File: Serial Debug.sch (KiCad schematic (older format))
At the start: 19 parts

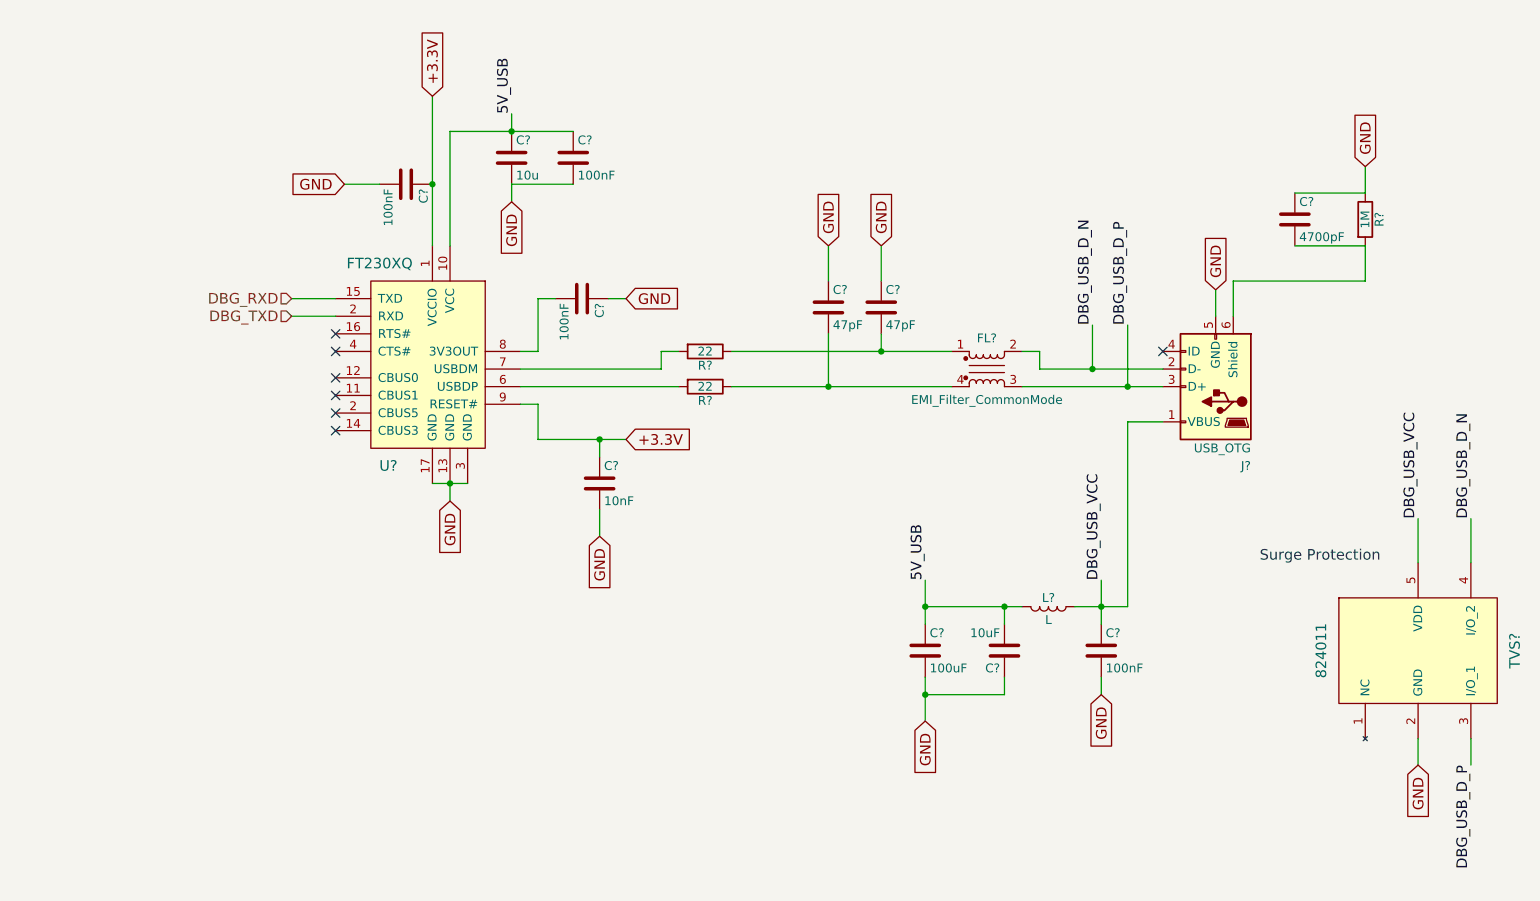
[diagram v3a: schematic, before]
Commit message: some issues fixed by the bugfixer; formal verification needed
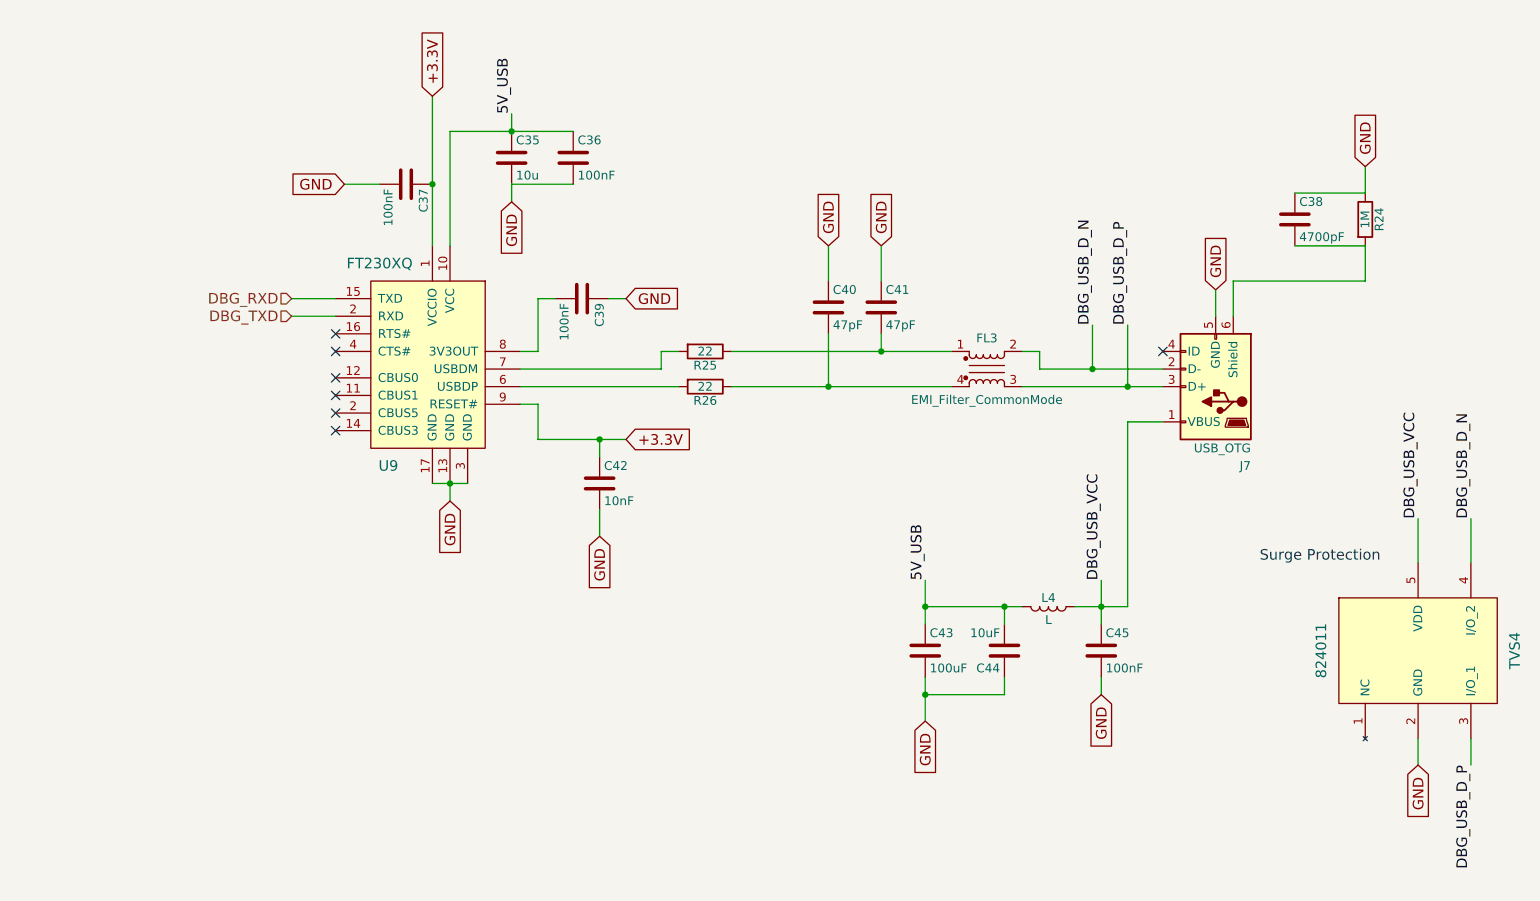
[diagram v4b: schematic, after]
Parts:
- gave numbers to parts that had none: 19
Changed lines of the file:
@@
 $EndDescr
 $Comp
-L FT230XQ U?
+L FT230XQ U9
 U 1 1 59A28254
 P 2450 2100
-F 0 "U?" H 2550 400 60  0000 C CNN
+F 0 "U9" H 2550 400 60  0000 C CNN
 F 1 "FT230XQ" H 2600 1550 60  0000 C CNN
 F 2 "" H 2450 2100 60  0001 C CNN
@@
 	3200 3450 3200 3650
 $Comp
-L R R?
+L R R25
 U 1 1 59A2A431
 P 4150 3150
-F 0 "R?" V 4230 3150 50  0000 C CNN
+F 0 "R25" V 4230 3150 50  0000 C CNN
 F 1 "22" V 4150 3150 50  0000 C CNN
 F 2 "" V 4080 3150 50  0001 C CNN
@@
 $EndComp
 $Comp
-L R R?
+L R R26
 U 1 1 59A2A466
 P 4150 3350
-F 0 "R?" V 4230 3350 50  0000 C CNN
+F 0 "R26" V 4230 3350 50  0000 C CNN
 F 1 "22" V 4150 3350 50  0000 C CNN
 F 2 "" V 4080 3350 50  0001 C CNN
@@
 $EndComp
 $Comp
-L EMI_Filter_CommonMode FL?
+L EMI_Filter_CommonMode FL3
 U 1 1 59A2AADC
 P 5750 3250
-F 0 "FL?" H 5750 3425 50  0000 C CNN
+F 0 "FL3" H 5750 3425 50  0000 C CNN
 F 1 "EMI_Filter_CommonMode" H 5750 3075 50  0000 C CNN
 F 2 "" V 5750 3290 50  0000 C CNN
@@
 	3100 3250 3900 3250
 $Comp
-L USB_OTG J?
+L USB_OTG J7
 U 1 1 59A2B35A
 P 7050 3350
-F 0 "J?" H 6850 3800 50  0000 L CNN
+F 0 "J7" H 6850 3800 50  0000 L CNN
 F 1 "USB_OTG" H 6850 3700 50  0000 L CNN
 F 2 "" H 7200 3300 50  0001 C CNN
@@
 GND
 $Comp
-L C C?
+L C C38
 U 1 1 59A2C300
 P 7500 2400
-F 0 "C?" H 7525 2500 50  0000 L CNN
+F 0 "C38" H 7525 2500 50  0000 L CNN
 F 1 "4700pF" H 7525 2300 50  0000 L CNN
 F 2 "" H 7538 2250 50  0001 C CNN
@@
 $EndComp
 $Comp
-L R R?
+L R R24
 U 1 1 59A2C331
 P 7900 2400
-F 0 "R?" V 7980 2400 50  0000 C CNN
+F 0 "R24" V 7980 2400 50  0000 C CNN
 F 1 "1M" V 7900 2400 50  0000 C CNN
 F 2 "" V 7830 2400 50  0001 C CNN
@@
 NoConn ~ 6750 3150
 $Comp
-L C C?
+L C C43
 U 1 1 59A2D00A
 P 5400 4850
-F 0 "C?" H 5425 4950 50  0000 L CNN
+F 0 "C43" H 5425 4950 50  0000 L CNN
 F 1 "100uF" H 5425 4750 50  0000 L CNN
 F 2 "" H 5438 4700 50  0001 C CNN
@@
 $EndComp
 $Comp
-L L L?
+L L L4
 U 1 1 59A2D09D
 P 6100 4600
-F 0 "L?" V 6050 4600 50  0000 C CNN
+F 0 "L4" V 6050 4600 50  0000 C CNN
 F 1 "L" V 6175 4600 50  0000 C CNN
 F 2 "" H 6100 4600 50  0001 C CNN
@@
 GND
 $Comp
-L C C?
+L C C41
 U 1 1 59A2FBBD
 P 5150 2900
-F 0 "C?" H 5175 3000 50  0000 L CNN
+F 0 "C41" H 5175 3000 50  0000 L CNN
 F 1 "47pF" H 5175 2800 50  0000 L CNN
 F 2 "" H 5188 2750 50  0001 C CNN
@@
 $EndComp
 $Comp
-L C C?
+L C C40
 U 1 1 59A2FC88
 P 4850 2900
-F 0 "C?" H 4875 3000 50  0000 L CNN
+F 0 "C40" H 4875 3000 50  0000 L CNN
 F 1 "47pF" H 4875 2800 50  0000 L CNN
 F 2 "" H 4888 2750 50  0001 C CNN
@@
 Connection ~ 4850 3350
 $Comp
-L 824011 TVS?
+L 824011 TVS4
 U 1 1 59A30AB4
 P 9050 4800
-F 0 "TVS?" V 8750 4750 60  0000 C CNN
+F 0 "TVS4" V 8750 4750 60  0000 C CNN
 F 1 "824011" V 7650 4750 60  0000 C CNN
 F 2 "" H 9050 4800 60  0001 C CNN
@@
 5V_USB
 $Comp
-L C C?
+L C C35
 U 1 1 59A63DF8
 P 3050 2050
-F 0 "C?" H 3075 2150 50  0000 L CNN
+F 0 "C35" H 3075 2150 50  0000 L CNN
 F 1 "10u" H 3075 1950 50  0000 L CNN
 F 2 "" H 3088 1900 50  0001 C CNN
@@
 	3900 3150 4000 3150
 $Comp
-L C C?
+L C C44
 U 1 1 59A86400
 P 5850 4850
-F 0 "C?" H 5875 4950 50  0000 L CNN
+F 0 "C44" H 5875 4950 50  0000 L CNN
 F 1 "10uF" H 5875 4750 50  0000 L CNN
 F 2 "Capacitors_SMD:C_0603_HandSoldering" H 5888 4700 30  0001 C CNN
@@
 Connection ~ 5850 4600
 $Comp
-L C C?
+L C C42
 U 1 1 59A67671
 P 3550 3900
-F 0 "C?" H 3575 4000 50  0000 L CNN
+F 0 "C42" H 3575 4000 50  0000 L CNN
 F 1 "10nF" H 3575 3800 50  0000 L CNN
 F 2 "Capacitors_SMD:C_0603_HandSoldering" H 3588 3750 50  0001 C CNN
@@
 $EndComp
 $Comp
-L C C?
+L C C39
 U 1 1 59A67F9E
 P 3450 2850
-F 0 "C?" H 3475 2950 50  0000 L CNN
+F 0 "C39" H 3475 2950 50  0000 L CNN
 F 1 "100nF" H 3475 2750 50  0000 L CNN
 F 2 "Capacitors_SMD:C_0603_HandSoldering" H 3488 2700 30  0001 C CNN
@@
 $EndComp
 $Comp
-L C C?
+L C C45
 U 1 1 59A68788
 P 6400 4850
-F 0 "C?" H 6425 4950 50  0000 L CNN
+F 0 "C45" H 6425 4950 50  0000 L CNN
 F 1 "100nF" H 6425 4750 50  0000 L CNN
 F 2 "Capacitors_SMD:C_0603_HandSoldering" H 6438 4700 30  0001 C CNN
@@
 $EndComp
 $Comp
-L C C?
+L C C36
 U 1 1 59A68F5E
 P 3400 2050
-F 0 "C?" H 3425 2150 50  0000 L CNN
+F 0 "C36" H 3425 2150 50  0000 L CNN
 F 1 "100nF" H 3425 1950 50  0000 L CNN
 F 2 "Capacitors_SMD:C_0603_HandSoldering" H 3438 1900 30  0001 C CNN
@@
 $EndComp
 $Comp
-L C C?
+L C C37
 U 1 1 59A69729
 P 2450 2200
-F 0 "C?" H 2475 2300 50  0000 L CNN
+F 0 "C37" H 2475 2300 50  0000 L CNN
 F 1 "100nF" H 2475 2100 50  0000 L CNN
 F 2 "Capacitors_SMD:C_0603_HandSoldering" H 2488 2050 30  0001 C CNN

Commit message: I have verified the schematic a second time (except the so-dimm), and I have selected all of the components with links and footprint. I need to verify the schematic a third time and root
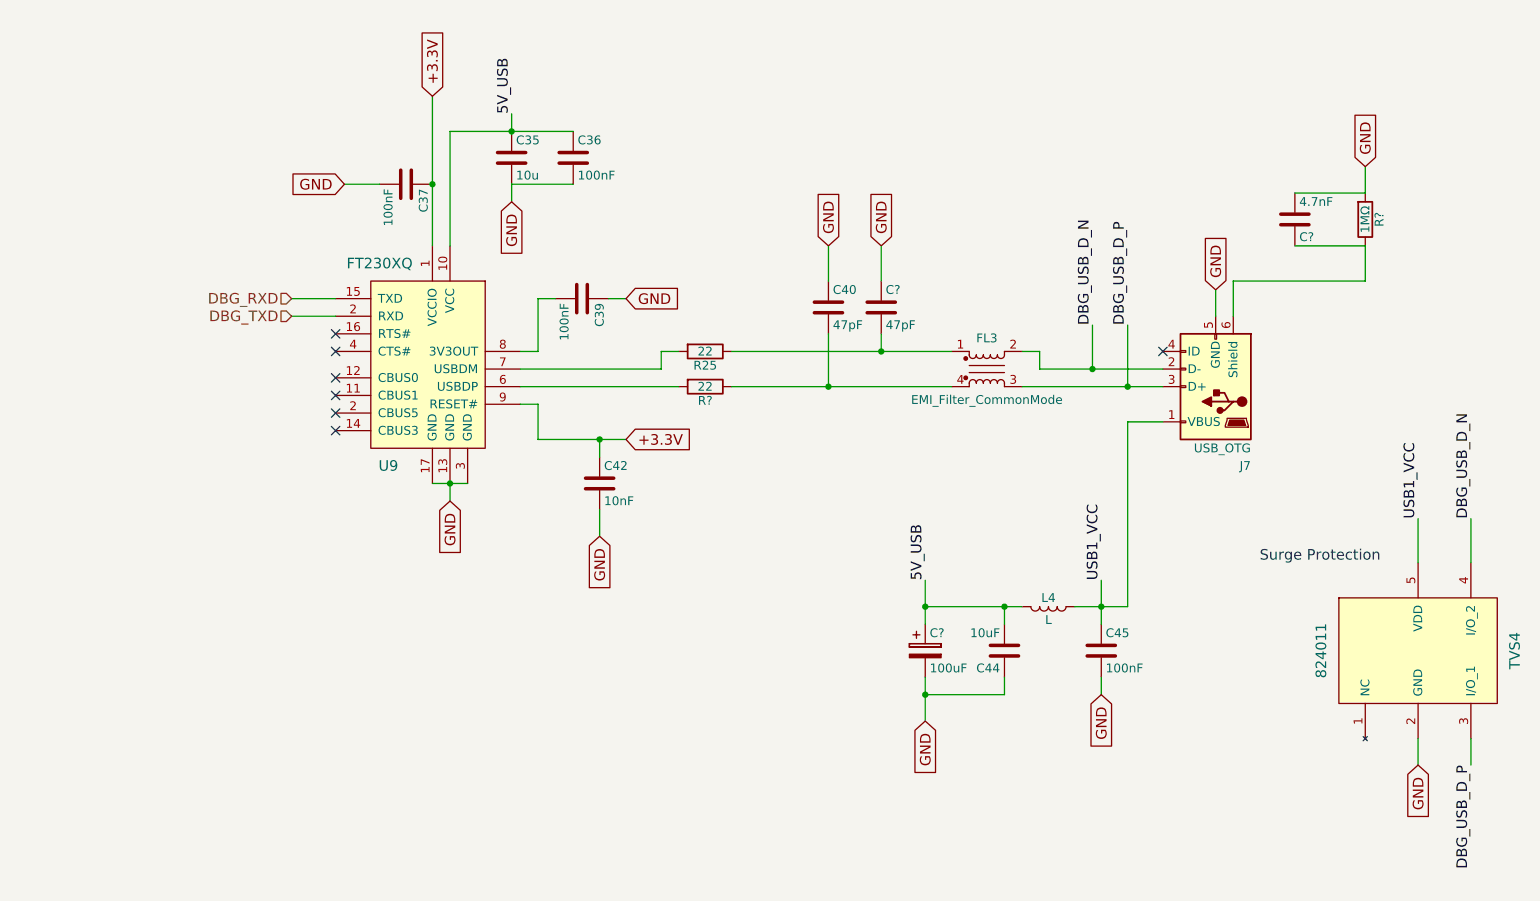
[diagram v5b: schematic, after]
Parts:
- removed C38: 4700pF, symbol C
- removed C41: 47pF, symbol C
- removed C43: 100uF, symbol C
- removed R24: 1M, symbol R
- removed R26: 22, symbol R
- added C?: 47pF, Capacitors_SMD:C_0603_HandSoldering, symbol C
- added C?: 4.7nF, Capacitors_SMD:C_0603_HandSoldering, symbol C
- added C?: 100uF, Capacitors_SMD:CP_Elec_6.3x5.7, symbol CP
- added R?: 22, Resistors_SMD:R_0603_HandSoldering, symbol R
- added R?: 1MΩ, Resistors_SMD:R_0603_HandSoldering, symbol R
- C40: footprint (none) -> Capacitors_SMD:C_0603_HandSoldering
- FL3: footprint (none) -> water:744233121
- J7: footprint (none) -> Connectors_USB:USB_Micro-B_Molex-105017-0001
- L4: footprint (none) -> Inductors_SMD:L_0603_HandSoldering
- R25: footprint (none) -> Resistors_SMD:R_0603_HandSoldering
- TVS4: footprint (none) -> Housings_SOT-23_SOT-143_TSOT-6:SOT-23-5
- U9: footprint (none) -> Housings_DFN_QFN:QFN-16-1EP_4x4mm_Pitch0.65mm
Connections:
- net 5V_USB: now also C?.1
- net GND: now also C?.1, C?.2, C?.2, R?.2
- net at U9.6 (USBDP): now also R?.2
- net at FL3.1, R25.1: now also C?.2
- net at C40.2, FL3.4: now also R?.1
- net at J7.6 (Shield): now also C?.1, R?.1
- net DBG_USB_VCC renamed USB1_VCC
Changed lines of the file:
@@
 F 0 "U9" H 2550 400 60  0000 C CNN
 F 1 "FT230XQ" H 2600 1550 60  0000 C CNN
-F 2 "" H 2450 2100 60  0001 C CNN
-F 3 "" H 2450 2100 60  0001 C CNN
+F 2 "Housings_DFN_QFN:QFN-16-1EP_4x4mm_Pitch0.65mm" H 2450 2100 60  0001 C CNN
+F 3 "http://hu.farnell.com/ftdi/ft230xq/i-f-usb2-0-fs-to-basic-uart-16qfn/dp/2081324" H 2450 2100 60  0001 C CNN
 	1    2450 2100
 	-1   0    0    -1
@@
 F 0 "R25" V 4230 3150 50  0000 C CNN
 F 1 "22" V 4150 3150 50  0000 C CNN
-F 2 "" V 4080 3150 50  0001 C CNN
-F 3 "" H 4150 3150 50  0001 C CNN
+F 2 "Resistors_SMD:R_0603_HandSoldering" V 4080 3150 50  0001 C CNN
+F 3 "http://hu.farnell.com/multicomp/mcwr06x22r0ftl/res-thick-film-22ohm-1-0-1w/dp/2447301" H 4150 3150 50  0001 C CNN
 	1    4150 3150
-	0    1    1    0
-$EndComp
-$Comp
-L R R26
-U 1 1 59A2A466
-P 4150 3350
-F 0 "R26" V 4230 3350 50  0000 C CNN
-F 1 "22" V 4150 3350 50  0000 C CNN
-F 2 "" V 4080 3350 50  0001 C CNN
-F 3 "" H 4150 3350 50  0001 C CNN
-	1    4150 3350
 	0    1    1    0
 $EndComp
@@
 F 0 "FL3" H 5750 3425 50  0000 C CNN
 F 1 "EMI_Filter_CommonMode" H 5750 3075 50  0000 C CNN
-F 2 "" V 5750 3290 50  0000 C CNN
+F 2 "water:744233121" V 5750 3290 50  0001 C CNN
 F 3 "http://hu.farnell.com/wurth-elektronik/744233121/line-filter-lvds-0805-120ohm-0/dp/1848957" V 5750 3290 50  0001 C CNN
 	1    5750 3250
@@
 F 0 "J7" H 6850 3800 50  0000 L CNN
 F 1 "USB_OTG" H 6850 3700 50  0000 L CNN
-F 2 "" H 7200 3300 50  0001 C CNN
-F 3 "" H 7200 3300 50  0001 C CNN
+F 2 "Connectors_USB:USB_Micro-B_Molex-105017-0001" H 7200 3300 50  0001 C CNN
+F 3 "http://hu.farnell.com/hirose-hrs/zx62d-b-5pa8-30/micro-usb-2-0-type-b-rcpt-smt/dp/2554981" H 7200 3300 50  0001 C CNN
 	1    7050 3350
 	-1   0    0    1
@@
 Text GLabel 7900 2100 1    60   Input ~ 0
 GND
-$Comp
-L C C38
-U 1 1 59A2C300
-P 7500 2400
-F 0 "C38" H 7525 2500 50  0000 L CNN
-F 1 "4700pF" H 7525 2300 50  0000 L CNN
-F 2 "" H 7538 2250 50  0001 C CNN
-F 3 "" H 7500 2400 50  0001 C CNN
-	1    7500 2400
-	1    0    0    -1
-$EndComp
-$Comp
-L R R24
-U 1 1 59A2C331
-P 7900 2400
-F 0 "R24" V 7980 2400 50  0000 C CNN
-F 1 "1M" V 7900 2400 50  0000 C CNN
-F 2 "" V 7830 2400 50  0001 C CNN
-F 3 "" H 7900 2400 50  0001 C CNN
-	1    7900 2400
-	1    0    0    -1
-$EndComp
-Wire Wire Line
-	7900 2100 7900 2250
-Wire Wire Line
-	7900 2250 7500 2250
-Wire Wire Line
-	7900 2550 7500 2550
-Wire Wire Line
-	7900 2550 7900 2750
 Wire Wire Line
 	7900 2750 7150 2750
@@
 	7050 2800 7050 2950
 NoConn ~ 6750 3150
-$Comp
-L C C43
-U 1 1 59A2D00A
-P 5400 4850
-F 0 "C43" H 5425 4950 50  0000 L CNN
-F 1 "100uF" H 5425 4750 50  0000 L CNN
-F 2 "" H 5438 4700 50  0001 C CNN
-F 3 "" H 5400 4850 50  0001 C CNN
-	1    5400 4850
-	1    0    0    -1
-$EndComp
 $Comp
 L L L4
@@
 F 0 "L4" V 6050 4600 50  0000 C CNN
 F 1 "L" V 6175 4600 50  0000 C CNN
-F 2 "" H 6100 4600 50  0001 C CNN
+F 2 "Inductors_SMD:L_0603_HandSoldering" H 6100 4600 50  0001 C CNN
 F 3 "http://hu.farnell.com/wurth-elektronik/742792641/ferrite-bead-0603-0-15ohm-2a/dp/1635705" H 6100 4600 50  0001 C CNN
 	1    6100 4600
@@
 Connection ~ 5400 4600
 Text Label 6400 4450 1    60   ~ 0
-DBG_USB_VCC
+USB1_VCC
 Connection ~ 6400 4600
 Wire Wire Line
@@
 Text GLabel 5150 2550 1    60   Input ~ 0
 GND
-$Comp
-L C C41
-U 1 1 59A2FBBD
-P 5150 2900
-F 0 "C41" H 5175 3000 50  0000 L CNN
-F 1 "47pF" H 5175 2800 50  0000 L CNN
-F 2 "" H 5188 2750 50  0001 C CNN
-F 3 "" H 5150 2900 50  0001 C CNN
-	1    5150 2900
-	1    0    0    -1
-$EndComp
 $Comp
 L C C40
@@
 F 0 "C40" H 4875 3000 50  0000 L CNN
 F 1 "47pF" H 4875 2800 50  0000 L CNN
-F 2 "" H 4888 2750 50  0001 C CNN
-F 3 "" H 4850 2900 50  0001 C CNN
+F 2 "Capacitors_SMD:C_0603_HandSoldering" H 4888 2750 50  0001 C CNN
+F 3 "http://hu.farnell.com/avx/06035a470jat2a/cap-mlcc-c0g-np0-47pf-50v-0603/dp/498567" H 4850 2900 50  0001 C CNN
 	1    4850 2900
 	1    0    0    -1
@@
 F 0 "TVS4" V 8750 4750 60  0000 C CNN
 F 1 "824011" V 7650 4750 60  0000 C CNN
-F 2 "" H 9050 4800 60  0001 C CNN
-F 3 "" H 9050 4800 60  0001 C CNN
+F 2 "Housings_SOT-23_SOT-143_TSOT-6:SOT-23-5" H 9050 4800 60  0001 C CNN
+F 3 "http://hu.farnell.com/wurth-elektronik/824011/diode-array-tvs/dp/1748616" H 9050 4800 60  0001 C CNN
 	1    9050 4800
 	1    0    0    -1
@@
 	8200 5500 8200 5350
 Text Label 8200 4100 1    60   ~ 0
-DBG_USB_VCC
+USB1_VCC
 Wire Wire Line
 	8200 4100 8200 4350
@@
 	0    1    1    0
 $EndComp
+$Comp
+L R R?
+U 1 1 59AA0F3A
+P 7900 2400
+F 0 "R?" V 7980 2400 50  0000 C CNN
+F 1 "1MΩ" V 7900 2400 50  0000 C CNN
+F 2 "Resistors_SMD:R_0603_HandSoldering" V 7830 2400 50  0001 C CNN
+F 3 "http://hu.farnell.com/multicomp/mcwr06x1004ftl/res-thick-film-1m-1-0-1w-0603/dp/2447285" H 7900 2400 50  0001 C CNN
+	1    7900 2400
+	1    0    0    1
+$EndComp
+$Comp
+L C C?
+U 1 1 59AA0F41
+P 7500 2400
+F 0 "C?" H 7525 2500 50  0000 L CNN
+F 1 "4.7nF" H 7525 2300 50  0000 L CNN
+F 2 "Capacitors_SMD:C_0603_HandSoldering" H 7538 2250 50  0001 C CNN
+F 3 "http://hu.farnell.com/avx/06035c472kat2a/cap-mlcc-x7r-4-7nf-50v-0603/dp/317263" H 7500 2400 50  0001 C CNN
+	1    7500 2400
+	1    0    0    1
+$EndComp
+Wire Wire Line
+	7900 2750 7900 2550
+Wire Wire Line
+	7900 2550 7500 2550
+Wire Wire Line
+	7500 2250 7900 2250
+Wire Wire Line
+	7900 2250 7900 2100
+$Comp
+L R R?
+U 1 1 59A9B327
+P 4150 3350
+F 0 "R?" V 4230 3350 50  0000 C CNN
+F 1 "22" V 4150 3350 50  0000 C CNN
+F 2 "Resistors_SMD:R_0603_HandSoldering" V 4080 3350 50  0001 C CNN
+F 3 "http://hu.farnell.com/multicomp/mcwr06x22r0ftl/res-thick-film-22ohm-1-0-1w/dp/2447301" H 4150 3350 50  0001 C CNN
+	1    4150 3350
+	0    1    1    0
+$EndComp
+$Comp
+L C C?
+U 1 1 59A9B888
+P 5150 2900
+F 0 "C?" H 5175 3000 50  0000 L CNN
+F 1 "47pF" H 5175 2800 50  0000 L CNN
+F 2 "Capacitors_SMD:C_0603_HandSoldering" H 5188 2750 50  0001 C CNN
+F 3 "http://hu.farnell.com/avx/06035a470jat2a/cap-mlcc-c0g-np0-47pf-50v-0603/dp/498567" H 5150 2900 50  0001 C CNN
+	1    5150 2900
+	1    0    0    -1
+$EndComp
+$Comp
+L CP C?
+U 1 1 59AA48F7
+P 5400 4850
+F 0 "C?" H 5425 4950 50  0000 L CNN
+F 1 "100uF" H 5425 4750 50  0000 L CNN
+F 2 "Capacitors_SMD:CP_Elec_6.3x5.7" H 5438 4700 50  0001 C CNN
+F 3 "http://hu.farnell.com/multicomp/mcvvt6r3m101da1l/cap-alu-elec-100uf-6-3v-rad-can/dp/2611414" H 5400 4850 50  0001 C CNN
+	1    5400 4850
+	1    0    0    -1
+$EndComp
 $EndSCHEMATC
